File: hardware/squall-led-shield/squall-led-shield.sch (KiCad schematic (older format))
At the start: 17 parts, among them J1 SQUALL_HEADER, J2 TC2030, Q1 Q_2NMOS

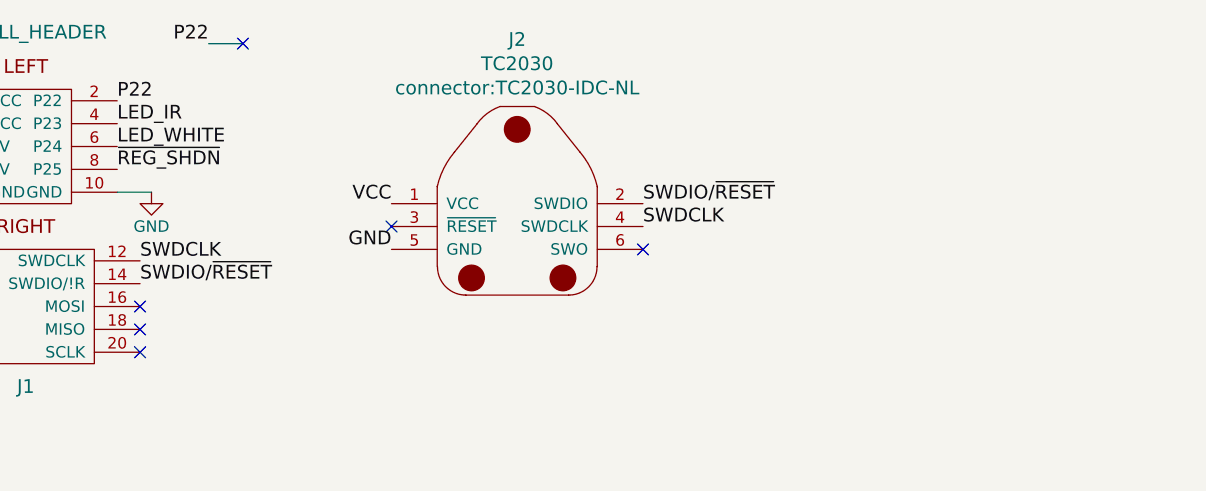
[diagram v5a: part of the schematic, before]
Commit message: Add tack pads for last gpio
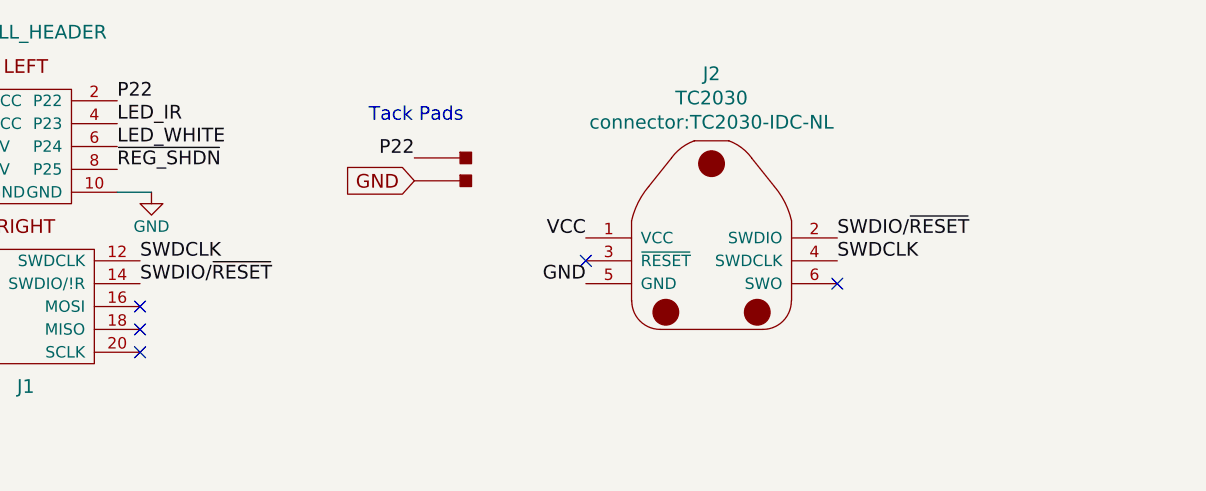
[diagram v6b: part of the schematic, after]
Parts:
- added J3, J4: TACK_PAD, Squall:TACK_PAD_FB_100MIL, symbol TACK_PAD
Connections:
- net GND: now also J4.1
- net P22: now also J3.1
- no-connect marks 12 -> 11
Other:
- note added: "Tack Pads"
- moved on the sheet: J2
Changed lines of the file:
@@
 L TC2030 J2
 U 1 1 5797C244
-P 4800 1450
-F 0 "J2" H 4800 2268 60  0000 C CNN
-F 1 "TC2030" H 4800 2162 60  0000 C CNN
-F 2 "connector:TC2030-IDC-NL" H 4800 2056 60  0000 C CNN
-F 3 "" H 4800 1450 60  0001 C CNN
-	1    4800 1450
+P 5650 1600
+F 0 "J2" H 5650 2418 60  0000 C CNN
+F 1 "TC2030" H 5650 2312 60  0000 C CNN
+F 2 "connector:TC2030-IDC-NL" H 5650 2206 60  0000 C CNN
+F 3 "" H 5650 1600 60  0001 C CNN
+	1    5650 1600
 	1    0    0    -1
 $EndComp
@@
 Text Label 3150 1700 0    60   ~ 0
 SWDIO/~RESET
-Text Label 5350 1350 0    60   ~ 0
+Text Label 6200 1500 0    60   ~ 0
 SWDIO/~RESET
-Text Label 5350 1450 0    60   ~ 0
+Text Label 6200 1600 0    60   ~ 0
 SWDCLK
-Text Label 4250 1350 2    60   ~ 0
+Text Label 5100 1500 2    60   ~ 0
 VCC
-Text Label 4250 1550 2    60   ~ 0
+Text Label 5100 1700 2    60   ~ 0
 GND
-NoConn ~ 5350 1550
-NoConn ~ 4250 1450
+NoConn ~ 6200 1700
+NoConn ~ 5100 1600
 Text Label 3050 1200 0    60   ~ 0
 ~REG_SHDN
 Text Label 3050 900  0    60   ~ 0
 P22
-Wire Wire Line
-	3450 650  3600 650
-Text Label 3450 650  2    60   ~ 0
+Text Label 4350 1150 2    60   ~ 0
 P22
-NoConn ~ 3600 650
+$Comp
+L TACK_PAD J3
+U 1 1 5797F0CF
+P 4550 1150
+F 0 "J3" H 4550 1025 60  0001 C CNN
+F 1 "TACK_PAD" H 4550 1250 60  0001 C CNN
+F 2 "Squall:TACK_PAD_FB_100MIL" H 4550 1150 60  0001 C CNN
+F 3 "" H 4550 1150 60  0001 C CNN
+	1    4550 1150
+	1    0    0    -1
+$EndComp
+$Comp
+L TACK_PAD J4
+U 1 1 5797F113
+P 4550 1250
+F 0 "J4" H 4550 1125 60  0001 C CNN
+F 1 "TACK_PAD" H 4550 1350 60  0001 C CNN
+F 2 "Squall:TACK_PAD_FB_100MIL" H 4550 1250 60  0001 C CNN
+F 3 "" H 4550 1250 60  0001 C CNN
+	1    4550 1250
+	1    0    0    -1
+$EndComp
+Text GLabel 4350 1250 0    60   Input ~ 0
+GND
+Text Notes 4150 1000 0    60   ~ 0
+Tack Pads
 $EndSCHEMATC

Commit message: Oops, save tack pad footprint in sch as well
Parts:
- J3, J4: footprint Squall:TACK_PAD_FB_100MIL -> Squall:TACK_PAD_FB_75MIL
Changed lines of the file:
@@
 F 0 "J3" H 4550 1025 60  0001 C CNN
 F 1 "TACK_PAD" H 4550 1250 60  0001 C CNN
-F 2 "Squall:TACK_PAD_FB_100MIL" H 4550 1150 60  0001 C CNN
+F 2 "Squall:TACK_PAD_FB_75MIL" H 4550 1150 60  0001 C CNN
 F 3 "" H 4550 1150 60  0001 C CNN
 	1    4550 1150
@@
 F 0 "J4" H 4550 1125 60  0001 C CNN
 F 1 "TACK_PAD" H 4550 1350 60  0001 C CNN
-F 2 "Squall:TACK_PAD_FB_100MIL" H 4550 1250 60  0001 C CNN
+F 2 "Squall:TACK_PAD_FB_75MIL" H 4550 1250 60  0001 C CNN
 F 3 "" H 4550 1250 60  0001 C CNN
 	1    4550 1250

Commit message: Add BOM
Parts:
- D1: Description (none) -> IR LED 850NM 1A; Digikey (none) -> VSMY7850X01-GS08CT-ND; MFN (none) -> Vishay; MFP (none) -> VSMY7850X01-GS08
- D2: Description (none) -> LED XLAMP COOL WHITE 6200K 2SMD; Digikey (none) -> XTEAWT-00-0000-000000G51CT-ND
- D3: Description (none) -> DIODE SCHOTTKY 20V 500MA SOD123; Digikey (none) -> MBR0520LT1GOSCT-ND; MFN (none) -> ON Semiconductor; MFP (none) -> MBR0520LT1G
- J1: Description (none) -> Header for a sensor board on top of the Squall BLE tag boar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; Digikey (none) -> H11617CT-ND
- L1: Description (none) -> 4.7µH Shielded Wirewound Inductor 740mA 190 mOhm Max Nonsta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; Digikey (none) -> 445-3225-1-ND; MFN (none) -> TDK-Corporation; MFP (none) -> VLF3012AT-4R7MR74
- Q1: Description (none) -> MOSFET 2N-CH 20V 1.3A SOT-363; Digikey (none) -> SI1922EDH-T1-GE3CT-ND
- R1: Description (none) -> RES SMD 68 OHM 5% 1/2W 0805; Digikey (none) -> P68ADCT-ND
- R2: Description (none) -> RES SMD 47 OHM 5% 1/2W 0805; Digikey (none) -> P47ADCT-ND
- VR1: Description (none) -> Boost Switching Regulator IC Positive Adjustable 2.5V 1 Out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; Digikey (none) -> 863-1495-1-ND; MFN (none) -> Skyworks-Solutions-Inc.; MFP (none) -> AAT1217ICA-1.2-T1
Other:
- moved on the sheet: J1
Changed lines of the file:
@@
 F 2 "Resistors_SMD:R_0805" V 1550 3150 50  0000 C CNN
 F 3 "" H 1700 3150 50  0000 C CNN
+F 4 "RES SMD 68 OHM 5% 1/2W 0805" V 1700 3150 60  0001 C CNN "Description"
+F 5 "P68ADCT-ND" V 1700 3150 60  0001 C CNN "Digikey"
 	1    1700 3150
 	0    1    1    0
@@
 L SQUALL_HEADER J1
 U 1 1 57916234
-P 2650 600
-F 0 "J1" H 2650 -950 60  0000 C CNN
-F 1 "SQUALL_HEADER" H 2650 600 60  0000 C CNN
-F 2 "Squall:SQUALL_HEADER" H 2650 600 60  0001 C CNN
-F 3 "" H 2650 600 60  0000 C CNN
-	1    2650 600
+P 2650 700
+F 0 "J1" H 2650 -850 60  0000 C CNN
+F 1 "SQUALL_HEADER" H 2650 850 60  0000 C CNN
+F 2 "Squall:SQUALL_HEADER" H 2650 750 60  0000 C CNN
+F 3 "" H 2650 700 60  0000 C CNN
+F 4 "Header for a sensor board on top of the Squall BLE tag board." H 2650 700 60  0001 C CNN "Description"
+F 5 "H11617CT-ND" H 2650 650 60  0000 C CNN "Digikey"
+	1    2650 700
 	1    0    0    -1
 $EndComp
@@
 L VCC #PWR01
 U 1 1 579162D4
-P 1950 800
-F 0 "#PWR01" H 1950 650 50  0001 C CNN
-F 1 "VCC" H 1950 950 50  0000 C CNN
-F 2 "" H 1950 800 50  0000 C CNN
-F 3 "" H 1950 800 50  0000 C CNN
-	1    1950 800
+P 1950 900
+F 0 "#PWR01" H 1950 750 50  0001 C CNN
+F 1 "VCC" H 1950 1050 50  0000 C CNN
+F 2 "" H 1950 900 50  0000 C CNN
+F 3 "" H 1950 900 50  0000 C CNN
+	1    1950 900
 	1    0    0    -1
 $EndComp
@@
 L GND #PWR02
 U 1 1 57916308
-P 2100 1300
-F 0 "#PWR02" H 2100 1050 50  0001 C CNN
-F 1 "GND" H 2100 1150 50  0000 C CNN
-F 2 "" H 2100 1300 50  0000 C CNN
-F 3 "" H 2100 1300 50  0000 C CNN
-	1    2100 1300
+P 2100 1400
+F 0 "#PWR02" H 2100 1150 50  0001 C CNN
+F 1 "GND" H 2100 1250 50  0000 C CNN
+F 2 "" H 2100 1400 50  0000 C CNN
+F 3 "" H 2100 1400 50  0000 C CNN
+	1    2100 1400
 	1    0    0    -1
 $EndComp
@@
 L GND #PWR03
 U 1 1 57916322
-P 3200 1300
-F 0 "#PWR03" H 3200 1050 50  0001 C CNN
-F 1 "GND" H 3200 1150 50  0000 C CNN
-F 2 "" H 3200 1300 50  0000 C CNN
-F 3 "" H 3200 1300 50  0000 C CNN
-	1    3200 1300
-	1    0    0    -1
-$EndComp
-NoConn ~ 2150 1600
+P 3200 1400
+F 0 "#PWR03" H 3200 1150 50  0001 C CNN
+F 1 "GND" H 3200 1250 50  0000 C CNN
+F 2 "" H 3200 1400 50  0000 C CNN
+F 3 "" H 3200 1400 50  0000 C CNN
+	1    3200 1400
+	1    0    0    -1
+$EndComp
 NoConn ~ 2150 1700
 NoConn ~ 2150 1800
 NoConn ~ 2150 1900
 NoConn ~ 2150 2000
-NoConn ~ 3150 1800
+NoConn ~ 2150 2100
 NoConn ~ 3150 1900
 NoConn ~ 3150 2000
+NoConn ~ 3150 2100
 $Comp
 L C C1
@@
 F 1 "4.7µH" V 6800 3550 50  0000 R CNN
 F 2 "Squall:INDUCTOR_VLF" V 6700 3400 50  0000 C CNN
-F 3 "" H 6600 3400 50  0000 C CNN
+F 3 "http://www.tdkkorea.co.kr/pro/down_pdf.php?No=75&real_file=12167968315.pdf" H 6600 3400 50  0001 C CNN
+F 4 "4.7µH Shielded Wirewound Inductor 740mA 190 mOhm Max Nonstandard" V 6600 3400 60  0001 C CNN "Description"
+F 5 "445-3225-1-ND" V 6600 3400 60  0001 C CNN "Digikey"
+F 6 "TDK-Corporation" V 6600 3400 60  0001 C CNN "MFN"
+F 7 "VLF3012AT-4R7MR74" V 6600 3400 60  0001 C CNN "MFP"
 	1    6600 3400
 	0    -1   -1   0
@@
 F 2 "Resistors_SMD:R_0805" V 1850 4500 50  0000 C CNN
 F 3 "" H 1700 4500 50  0000 C CNN
+F 4 "RES SMD 47 OHM 5% 1/2W 0805" V 1700 4500 60  0001 C CNN "Description"
+F 5 "P47ADCT-ND" V 1700 4500 60  0001 C CNN "Digikey"
 	1    1700 4500
 	0    -1   -1   0
 $EndComp
-Text Label 3050 1000 0    60   ~ 0
+Text Label 3050 1100 0    60   ~ 0
 LED_IR
-Text Label 3050 1100 0    60   ~ 0
+Text Label 3050 1200 0    60   ~ 0
 LED_WHITE
 Text Label 6600 3900 2    60   ~ 0
@@
 F 1 "LED_HIGH_POWER" H 2500 4714 50  0000 C CNN
 F 2 "Squall:CREE_XT-E" H 2500 4623 50  0000 C CNN
-F 3 "" H 2500 4500 50  0000 C CNN
+F 3 "http://www.cree.com/~/media/Files/Cree/LED%20Components%20and%20Modules/XLamp/Data%20and%20Binning/XLampXTE" H 2500 4500 50  0001 C CNN
+F 4 "LED XLAMP COOL WHITE 6200K 2SMD" H 2500 4500 60  0001 C CNN "Description"
+F 5 "XTEAWT-00-0000-000000G51CT-ND" H 2500 4500 60  0001 C CNN "Digikey"
 	1    2500 4500
 	-1   0    0    -1
@@
 F 1 "Q_2NMOS" H 3039 3500 60  0000 L CNN
 F 2 "TO_SOT_Packages_SMD:SC-70-6" H 3039 3394 60  0000 L CNN
-F 3 "" H 3225 3600 60  0001 C CNN
+F 3 "http://www.vishay.com/docs/67192/si1922ed.pdf" H 3225 3600 60  0001 C CNN
+F 4 "MOSFET 2N-CH 20V 1.3A SOT-363" H 2850 3500 60  0001 C CNN "Description"
+F 5 "SI1922EDH-T1-GE3CT-ND" H 2850 3500 60  0001 C CNN "Digikey"
 	1    2850 3500
 	1    0    0    -1
@@
 F 1 "LED" H 2500 3364 50  0000 C CNN
 F 2 "Squall:VSMY785X" H 2500 3273 50  0000 C CNN
-F 3 "" H 2500 3150 50  0000 C CNN
+F 3 "http://www.vishay.com/docs/81145/vsmy7850.pdf" H 2500 3150 50  0001 C CNN
+F 4 "IR LED 850NM 1A" H 2500 3150 60  0001 C CNN "Description"
+F 5 "VSMY7850X01-GS08CT-ND" H 2500 3150 60  0001 C CNN "Digikey"
+F 6 "Vishay" H 2500 3150 60  0001 C CNN "MFN"
+F 7 "VSMY7850X01-GS08" H 2500 3150 60  0001 C CNN "MFP"
 	1    2500 3150
 	-1   0    0    -1
@@
 F 1 "AAT1217" H 7450 4100 60  0000 C CNN
 F 2 "TO_SOT_Packages_SMD:SOT-23-6" H 6950 3850 60  0001 C CNN
-F 3 "" H 6950 3850 60  0001 C CNN
+F 3 "http://www.skyworksinc.com/uploads/documents/AAT1217_202050B.pdf" H 6950 3850 60  0001 C CNN
+F 4 "Boost Switching Regulator IC Positive Adjustable 2.5V 1 Output 750mA (Switch) SOT-23-6 Thin, TSOT-23-6" H 7150 3850 60  0001 C CNN "Description"
+F 5 "863-1495-1-ND" H 7150 3850 60  0001 C CNN "Digikey"
+F 6 "Skyworks-Solutions-Inc." H 7150 3850 60  0001 C CNN "MFN"
+F 7 "AAT1217ICA-1.2-T1" H 7150 3850 60  0001 C CNN "MFP"
 	1    7150 3850
 	1    0    0    -1
@@
 Wire Wire Line
 	7150 4250 7150 4400
-Connection ~ 1950 900
-Wire Wire Line
-	1950 900  2250 900
+Connection ~ 1950 1000
 Wire Wire Line
 	1950 1000 2250 1000
 Wire Wire Line
-	1950 800  1950 1000
-Wire Wire Line
-	3050 1300 3200 1300
-Wire Wire Line
-	2250 1300 2100 1300
+	1950 1100 2250 1100
+Wire Wire Line
+	1950 900  1950 1100
+Wire Wire Line
+	3050 1400 3200 1400
+Wire Wire Line
+	2250 1400 2100 1400
 $Comp
 L D_Schottky D3
@@
 F 1 "D_Schottky" H 7700 3615 50  0000 C CNN
 F 2 "Diodes_SMD:SOD-123" H 7700 3524 50  0000 C CNN
-F 3 "" H 7700 3400 50  0000 C CNN
+F 3 "http://www.onsemi.com/pub_link/Collateral/MBR0520LT1-D.PDF" H 7700 3400 50  0001 C CNN
+F 4 "DIODE SCHOTTKY 20V 500MA SOD123" H 7700 3400 60  0001 C CNN "Description"
+F 5 "MBR0520LT1GOSCT-ND" H 7700 3400 60  0001 C CNN "Digikey"
+F 6 "ON Semiconductor" H 7700 3400 60  0001 C CNN "MFN"
+F 7 "MBR0520LT1G" H 7700 3400 60  0001 C CNN "MFP"
 	1    7700 3400
 	-1   0    0    -1
@@
 	7850 3400 8300 3400
 Connection ~ 8300 3450
+Text Label 2250 1300 2    60   ~ 0
+SQUALL_5V
 Text Label 2250 1200 2    60   ~ 0
-SQUALL_5V
-Text Label 2250 1100 2    60   ~ 0
 SQUALL_5V
 Text Label 6950 3400 0    60   ~ 0
@@
 	1    0    0    -1
 $EndComp
-Text Label 3150 1600 0    60   ~ 0
+Text Label 3150 1700 0    60   ~ 0
 SWDCLK
-Text Label 3150 1700 0    60   ~ 0
+Text Label 3150 1800 0    60   ~ 0
 SWDIO/~RESET
 Text Label 6200 1500 0    60   ~ 0
@@
 NoConn ~ 6200 1700
 NoConn ~ 5100 1600
-Text Label 3050 1200 0    60   ~ 0
+Text Label 3050 1300 0    60   ~ 0
 ~REG_SHDN
-Text Label 3050 900  0    60   ~ 0
+Text Label 3050 1000 0    60   ~ 0
 P22
 Text Label 4350 1150 2    60   ~ 0
